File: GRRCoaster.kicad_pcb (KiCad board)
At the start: 2 copper layers, 59.7 x 59.7 mm, 1 part

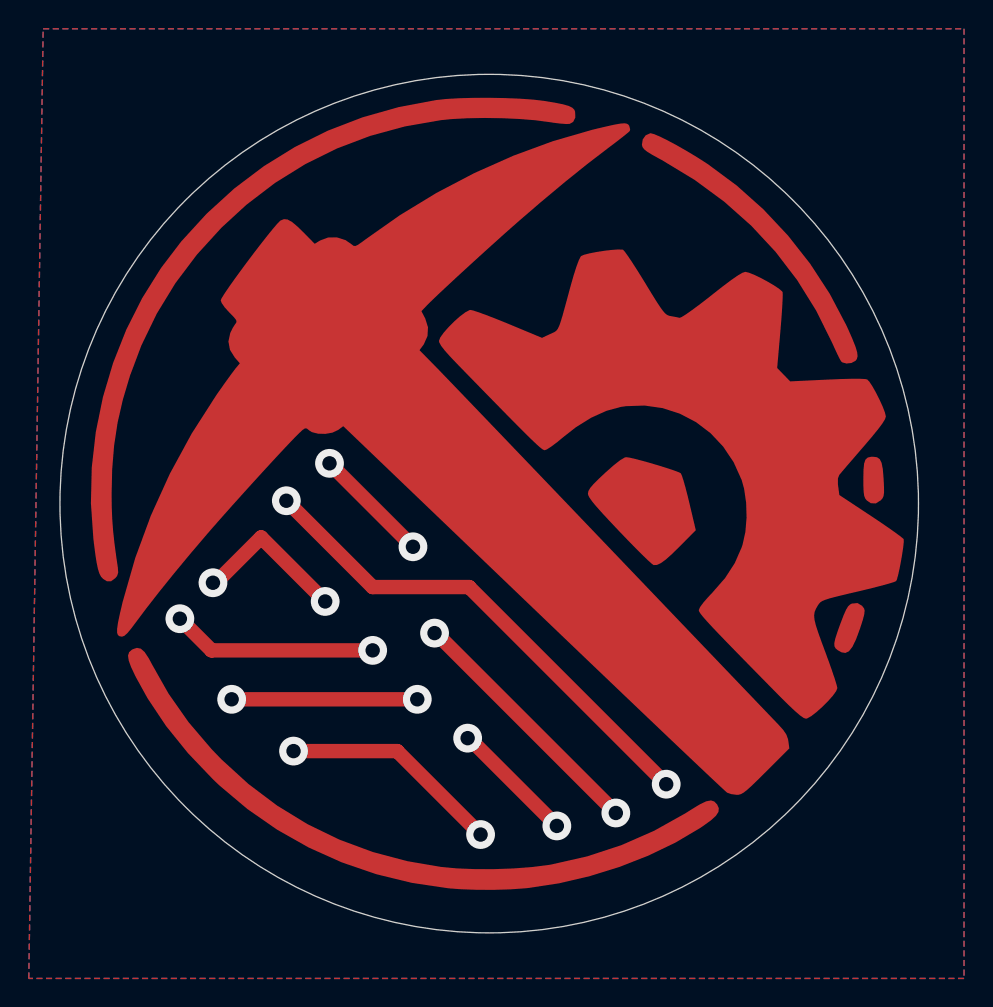
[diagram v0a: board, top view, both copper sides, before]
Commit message: centered logo
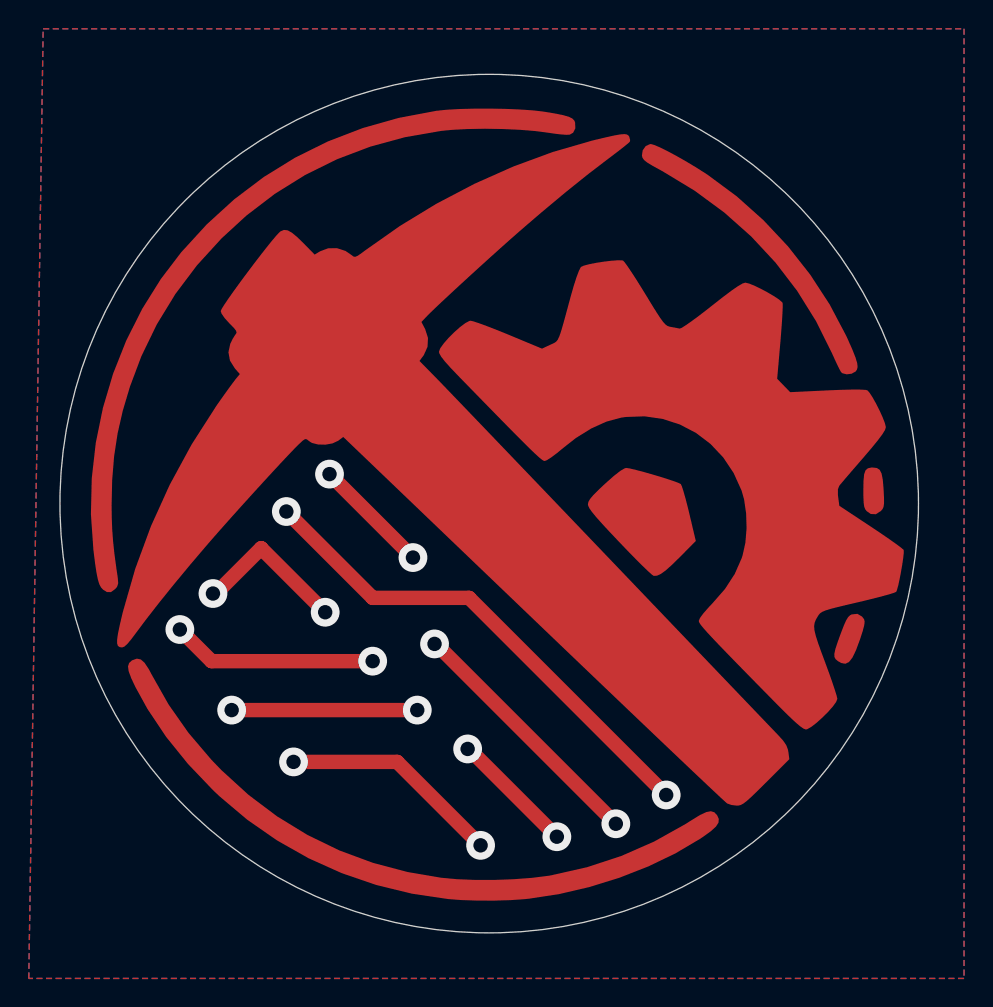
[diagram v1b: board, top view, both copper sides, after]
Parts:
- moved REF** 0.75 mm to (46.0, 77.8)
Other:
- board text added: "GRR"
- board text removed: "GOLD RUSH ROBOTICS"
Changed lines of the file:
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@@
 	(footprint "GRR:GRR_LARGE_1"
 		(layer "F.Cu")
-		(at 46 77)
+		(at 46 77.75)
 		(property "Reference" "REF**"
 			(at 0 -0.5 0)
@@
 		(layer "Edge.Cuts")
 	)
-	(gr_text " GOLD \nRUSH\nROBOTICS"
-		(at 47 61 0)
+	(gr_text "GRR"
+		(at 47.5648 42 0)
 		(layer "B.SilkS")
 		(effects
 			(font
-				(size 7 7)
-				(thickness 0.8)
+				(size 10 10)
+				(thickness 1)
 			)
 			(justify bottom mirror)
@@
 	)
 	(segment
-		(start 45.5 63.3)
-		(end 45.6 63.3)
-		(width 1)
-		(layer "F.Cu")
-		(net 0)
-	)
-	(segment
-		(start 31.15 49.35)
-		(end 35.6 53.8)
-		(width 1)
-		(layer "F.Cu")
-		(net 0)
-	)
-	(segment
-		(start 28 52.5)
-		(end 31.15 49.35)
-		(width 1)
-		(layer "F.Cu")
-		(net 0)
-	)
-	(segment
-		(start 27.8 52.5)
-		(end 28 52.5)
-		(width 1)
-		(layer "F.Cu")
-		(net 0)
-	)
-	(segment
-		(start 40.6 64.2)
-		(end 46.4 70)
-		(width 1)
-		(layer "F.Cu")
-		(net 0)
-	)
-	(segment
-		(start 32.9 46.8)
-		(end 38.9 52.8)
-		(width 1)
-		(layer "F.Cu")
-		(net 0)
-	)
-	(segment
-		(start 27.7 57.2)
-		(end 25.5 55)
-		(width 1)
-		(layer "F.Cu")
-		(net 0)
-	)
-	(segment
-		(start 38.9 57.2)
-		(end 27.7 57.2)
-		(width 1)
-		(layer "F.Cu")
-		(net 0)
-	)
-	(segment
-		(start 45.6 52.8)
-		(end 59.3 66.5)
-		(width 1)
-		(layer "F.Cu")
-		(net 0)
-	)
-	(segment
-		(start 41.7 50)
-		(end 35.9 44.2)
-		(width 1)
-		(layer "F.Cu")
-		(net 0)
-	)
-	(segment
-		(start 45.6 63.3)
-		(end 51.7 69.4)
-		(width 1)
-		(layer "F.Cu")
-		(net 0)
-	)
-	(segment
-		(start 43.3 56)
-		(end 43.2 56)
-		(width 1)
-		(layer "F.Cu")
-		(net 0)
-	)
-	(segment
-		(start 33.4 64.2)
-		(end 40.6 64.2)
-		(width 1)
-		(layer "F.Cu")
-		(net 0)
-	)
-	(segment
-		(start 29.1 60.6)
-		(end 42 60.6)
-		(width 1)
-		(layer "F.Cu")
-		(net 0)
-	)
-	(segment
-		(start 38.9 52.8)
-		(end 45.6 52.8)
-		(width 1)
-		(layer "F.Cu")
-		(net 0)
-	)
-	(segment
-		(start 55.8 68.5)
-		(end 43.3 56)
-		(width 1)
-		(layer "F.Cu")
-		(net 0)
-	)
-	(via
-		(at 27.8 52.5)
-		(size 2)
-		(drill 1)
-		(layers "F.Cu" "B.Cu")
-		(net 0)
-	)
-	(via
-		(at 59.3 66.5)
-		(size 2)
-		(drill 1)
-		(layers "F.Cu" "B.Cu")
-		(net 0)
-	)
-	(via
-		(at 51.7 69.4)
-		(size 2)
-		(drill 1)
-		(layers "F.Cu" "B.Cu")
-		(net 0)
-	)
-	(via
-		(at 45.5 63.3)
-		(size 2)
-		(drill 1)
-		(layers "F.Cu" "B.Cu")
-		(net 0)
-	)
-	(via
-		(at 46.4 70)
-		(size 2)
-		(drill 1)
-		(layers "F.Cu" "B.Cu")
-		(net 0)
-	)
-	(via
-		(at 55.8 68.5)
-		(size 2)
-		(drill 1)
-		(layers "F.Cu" "B.Cu")
-		(net 0)
-	)
-	(via
-		(at 42 60.6)
-		(size 2)
-		(drill 1)
-		(layers "F.Cu" "B.Cu")
-		(net 0)
-	)
-	(via
-		(at 25.5 55)
-		(size 2)
-		(drill 1)
-		(layers "F.Cu" "B.Cu")
-		(net 0)
-	)
-	(via
-		(at 33.4 64.2)
-		(size 2)
-		(drill 1)
-		(layers "F.Cu" "B.Cu")
-		(net 0)
-	)
-	(via
-		(at 38.9 57.2)
-		(size 2)
-		(drill 1)
-		(layers "F.Cu" "B.Cu")
-		(net 0)
-	)
-	(via
-		(at 35.6 53.8)
-		(size 2)
-		(drill 1)
-		(layers "F.Cu" "B.Cu")
-		(net 0)
-	)
-	(via
-		(at 29.1 60.6)
-		(size 2)
-		(drill 1)
-		(layers "F.Cu" "B.Cu")
-		(net 0)
-	)
-	(via
-		(at 32.9 46.8)
-		(size 2)
-		(drill 1)
-		(layers "F.Cu" "B.Cu")
-		(net 0)
-	)
-	(via
-		(at 43.2 56)
-		(size 2)
-		(drill 1)
-		(layers "F.Cu" "B.Cu")
-		(net 0)
-	)
-	(via
-		(at 41.7 50)
-		(size 2)
-		(drill 1)
-		(layers "F.Cu" "B.Cu")
-		(net 0)
-	)
-	(via
-		(at 35.9 44.2)
-		(size 2)
-		(drill 1)
+		(start 45.5 64.05)
+		(end 45.6 64.05)
+		(width 1)
+		(layer "F.Cu")
+		(net 0)
+	)
+	(segment
+		(start 31.15 50.1)
+		(end 35.6 54.55)
+		(width 1)
+		(layer "F.Cu")
+		(net 0)
+	)
+	(segment
+		(start 28 53.25)
+		(end 31.15 50.1)
+		(width 1)
+		(layer "F.Cu")
+		(net 0)
+	)
+	(segment
+		(start 27.8 53.25)
+		(end 28 53.25)
+		(width 1)
+		(layer "F.Cu")
+		(net 0)
+	)
+	(segment
+		(start 40.6 64.95)
+		(end 46.4 70.75)
+		(width 1)
+		(layer "F.Cu")
+		(net 0)
+	)
+	(segment
+		(start 32.9 47.55)
+		(end 38.9 53.55)
+		(width 1)
+		(layer "F.Cu")
+		(net 0)
+	)
+	(segment
+		(start 27.7 57.95)
+		(end 25.5 55.75)
+		(width 1)
+		(layer "F.Cu")
+		(net 0)
+	)
+	(segment
+		(start 38.9 57.95)
+		(end 27.7 57.95)
+		(width 1)
+		(layer "F.Cu")
+		(net 0)
+	)
+	(segment
+		(start 45.6 53.55)
+		(end 59.3 67.25)
+		(width 1)
+		(layer "F.Cu")
+		(net 0)
+	)
+	(segment
+		(start 41.7 50.75)
+		(end 35.9 44.95)
+		(width 1)
+		(layer "F.Cu")
+		(net 0)
+	)
+	(segment
+		(start 45.6 64.05)
+		(end 51.7 70.15)
+		(width 1)
+		(layer "F.Cu")
+		(net 0)
+	)
+	(segment
+		(start 43.3 56.75)
+		(end 43.2 56.75)
+		(width 1)
+		(layer "F.Cu")
+		(net 0)
+	)
+	(segment
+		(start 33.4 64.95)
+		(end 40.6 64.95)
+		(width 1)
+		(layer "F.Cu")
+		(net 0)
+	)
+	(segment
+		(start 29.1 61.35)
+		(end 42 61.35)
+		(width 1)
+		(layer "F.Cu")
+		(net 0)
+	)
+	(segment
+		(start 38.9 53.55)
+		(end 45.6 53.55)
+		(width 1)
+		(layer "F.Cu")
+		(net 0)
+	)
+	(segment
+		(start 55.8 69.25)
+		(end 43.3 56.75)
+		(width 1)
+		(layer "F.Cu")
+		(net 0)
+	)
+	(via
+		(at 27.8 53.25)
+		(size 2)
+		(drill 1)
+		(layers "F.Cu" "B.Cu")
+		(net 0)
+	)
+	(via
+		(at 59.3 67.25)
+		(size 2)
+		(drill 1)
+		(layers "F.Cu" "B.Cu")
+		(net 0)
+	)
+	(via
+		(at 51.7 70.15)
+		(size 2)
+		(drill 1)
+		(layers "F.Cu" "B.Cu")
+		(net 0)
+	)
+	(via
+		(at 45.5 64.05)
+		(size 2)
+		(drill 1)
+		(layers "F.Cu" "B.Cu")
+		(net 0)
+	)
+	(via
+		(at 46.4 70.75)
+		(size 2)
+		(drill 1)
+		(layers "F.Cu" "B.Cu")
+		(net 0)
+	)
+	(via
+		(at 55.8 69.25)
+		(size 2)
+		(drill 1)
+		(layers "F.Cu" "B.Cu")
+		(net 0)
+	)
+	(via
+		(at 42 61.35)
+		(size 2)
+		(drill 1)
+		(layers "F.Cu" "B.Cu")
+		(net 0)
+	)
+	(via
+		(at 25.5 55.75)
+		(size 2)
+		(drill 1)
+		(layers "F.Cu" "B.Cu")
+		(net 0)
+	)
+	(via
+		(at 33.4 64.95)
+		(size 2)
+		(drill 1)
+		(layers "F.Cu" "B.Cu")
+		(net 0)
+	)
+	(via
+		(at 38.9 57.95)
+		(size 2)
+		(drill 1)
+		(layers "F.Cu" "B.Cu")
+		(net 0)
+	)
+	(via
+		(at 35.6 54.55)
+		(size 2)
+		(drill 1)
+		(layers "F.Cu" "B.Cu")
+		(net 0)
+	)
+	(via
+		(at 29.1 61.35)
+		(size 2)
+		(drill 1)
+		(layers "F.Cu" "B.Cu")
+		(net 0)
+	)
+	(via
+		(at 32.9 47.55)
+		(size 2)
+		(drill 1)
+		(layers "F.Cu" "B.Cu")
+		(net 0)
+	)
+	(via
+		(at 43.2 56.75)
+		(size 2)
+		(drill 1)
+		(layers "F.Cu" "B.Cu")
+		(net 0)
+	)
+	(via
+		(at 41.7 50.75)
+		(size 2)
+		(drill 1)
+		(layers "F.Cu" "B.Cu")
+		(net 0)
+	)
+	(via
+		(at 35.9 44.95)
+		(size 2)
+		(drill 1)
